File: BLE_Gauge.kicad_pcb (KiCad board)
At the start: 4 copper layers, 53.3 x 50.2 mm, 31 parts, among them J1 TagConnect_TC2030-NL, J2 USB_C_Receptacle_PowerOnly_6P, U1 nRF54L15-QFXX, U2 LSM6DS3, X1 32MHz, X2 32.768kHz

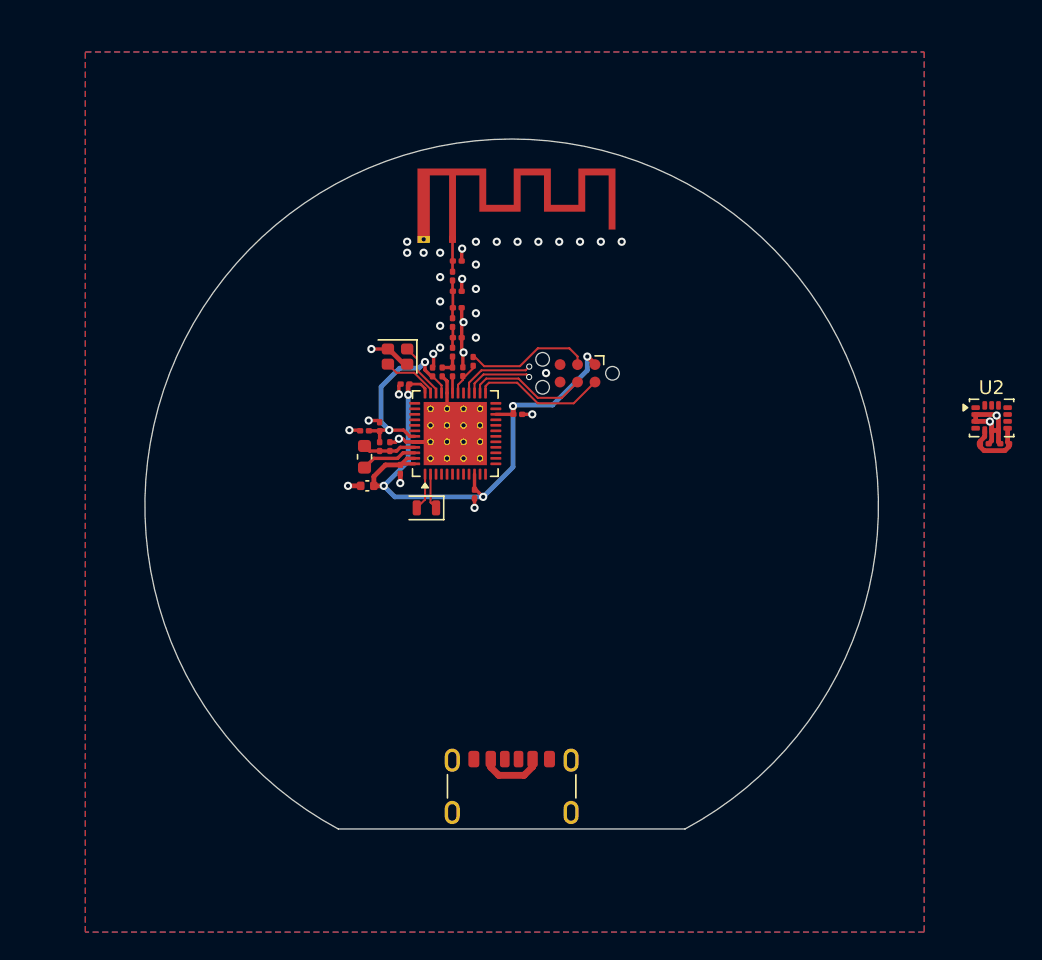
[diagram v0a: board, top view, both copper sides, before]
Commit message: Add Display
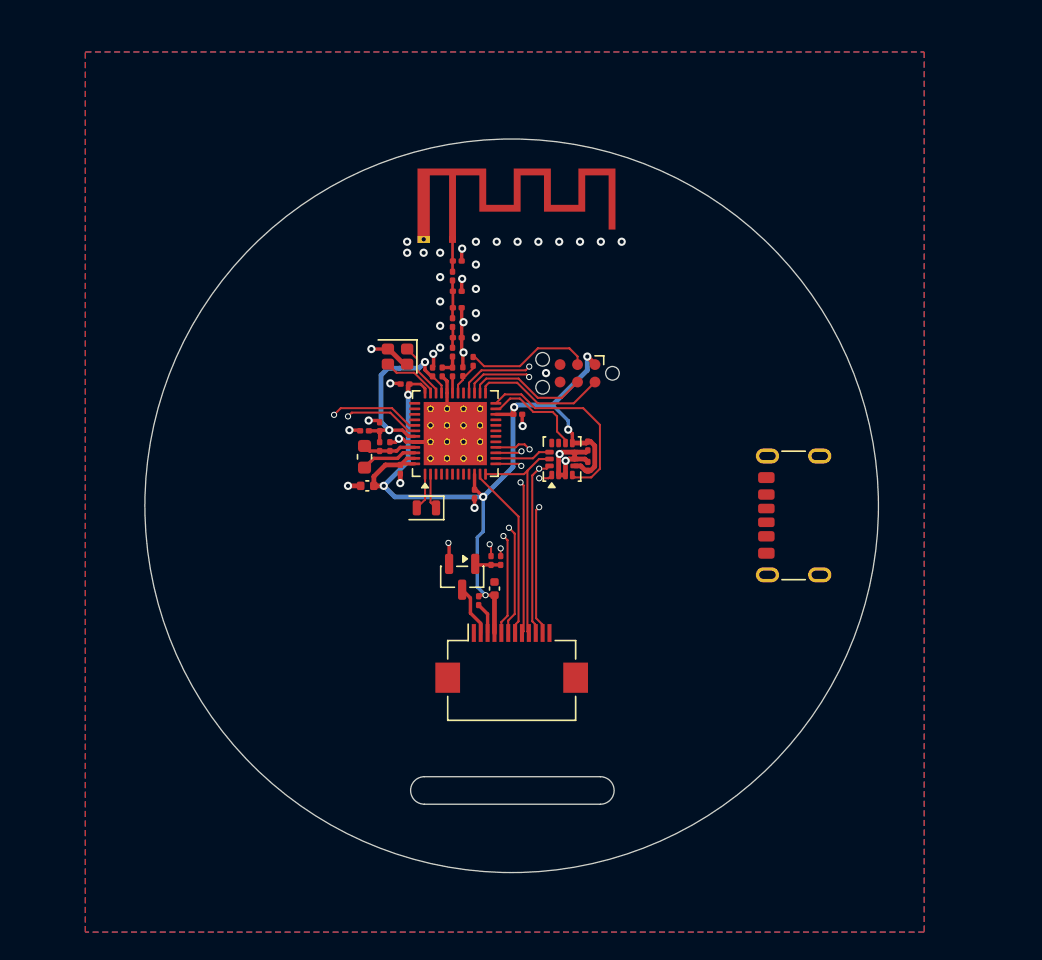
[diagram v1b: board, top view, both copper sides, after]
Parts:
- added C16: 10uF, Capacitor_SMD:C_0402_1005Metric, F.Cu at (147.2, 111.0)
- added J3: Conn_01x12_MountingPin, Connector_FFC-FPC:Hirose_FH12-12S-0.5SH_1x12-1MP_P0.50mm_Horizontal, F.Cu at (148.5, 116.1)
- added Q1: SS8050, Package_TO_SOT_SMD:SOT-23, F.Cu at (144.9, 110.2)
- added R2: 5.1k, Resistor_SMD:R_0201_0603Metric, F.Cu at (146.1, 111.9)
- added R3: 2.2k, Resistor_SMD:R_0201_0603Metric, F.Cu at (147.7, 109.0)
- added R4: 10k, Resistor_SMD:R_0201_0603Metric, F.Cu at (147.0, 109.0)
- moved U2 31.4 mm to (152.2, 101.6), turned to 90 degrees
- moved C15 30.3 mm to (154.0, 100.6), turned to -90 degrees
- moved J2 30.0 mm to (170.1, 105.7), turned to 90 degrees
- moved C14 28.9 mm to (154.0, 102.1), turned to 90 degrees
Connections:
- U1 pad 11: unconnected-(U1-P2.00-Pad11) -> /DC.DISP
- U1 pad 12: unconnected-(U1-P2.01-Pad12) -> /SPI_SCK
- U1 pad 13: unconnected-(U1-P2.02-Pad13) -> /SPI_MISO
- U1 pad 14: unconnected-(U1-P2.03-Pad14) -> /CS.LSM6
- U1 pad 15: unconnected-(U1-P2.04-Pad15) -> /SPI_MOSI
- U1 pad 16: unconnected-(U1-P2.05-Pad16) -> /CS.DISP
- U1 pad 23: unconnected-(U1-P0.00-Pad23) -> /INT2.LSM6
- U1 pad 24: unconnected-(U1-P0.01-Pad24) -> /INT1.LSM6
- U1 pad 28: unconnected-(U1-P0.03-Pad28) -> /BL.DISP
- U1 pad 29: unconnected-(U1-P0.04-Pad29) -> /INT.nPM
- U1 pad 39: unconnected-(U1-P1.11-Pad39) -> /SDA
- U1 pad 40: unconnected-(U1-P1.12-Pad40) -> /SCL
- U1 pad 41: unconnected-(U1-P1.13-Pad41) -> /RST.DISP
- U1 pad 42: unconnected-(U1-P1.14-Pad42) -> /TE.DISP
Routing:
- net /RST.DISP: track 0.00 -> 40.1 mm, vias 0 -> 2
- net /TE.DISP: track 0.00 -> 34.4 mm, vias 0 -> 2
- net /BL.DISP: track 0.00 -> 20.5 mm, vias 0 -> 2
- net /CS.DISP: track 0.00 -> 17.8 mm, vias 0 -> 2
- net /SPI_MISO: track 0.00 -> 17.3 mm, vias 0 -> 3
- net /SPI_SCK: track 0.00 -> 17.0 mm
- net /SPI_MOSI: track 0.00 -> 16.8 mm, vias 0 -> 2
- net VDD: track 47.9 -> 62.6 mm, vias 5 -> 7
- net /INT1.LSM6: track 0.00 -> 14.3 mm
- net /DC.DISP: track 0.00 -> 12.8 mm
- net /INT2.LSM6: track 0.00 -> 7.49 mm
- net unconnected-(U1-P0.03-Pad28): track 5.61 -> 0.00 mm, vias 1 -> 0
- net Net-(J2-VBUS-PadA9): track 4.70 -> 0.00 mm
- net /CS.LSM6: track 0.00 -> 4.09 mm
- net Net-(J3-Pin_2): track 0.00 -> 3.71 mm
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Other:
- board size 53.3 x 50.2 mm -> 53.3 x 53.3 mm

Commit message: Arrumando bagunça
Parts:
- C1: footprint Capacitor_SMD:C_0402_1005Metric -> Nath:C_0402_1005Metric_Nordic
- C10, C11, C12, C13, C2, C3, C6, C7, C8, C9: footprint Capacitor_SMD:C_0201_0603Metric -> Nath:C_0201_0603Metric_Nordic
- C4: value 3.9pF -> 2.2uF; footprint Capacitor_SMD:C_0201_0603Metric -> Nath:C_0201_0603Metric_Nordic
- C5: value 2.2uF -> 3.9pF; footprint Capacitor_SMD:C_0201_0603Metric -> Nath:C_0201_0603Metric_Nordic
- FB1: value 100R@100MHz -> 120R/0.2A; footprint Inductor_SMD:L_0201_0603Metric -> Nath:L_0201_0603Metric_Nordic
- L1: footprint Inductor_SMD:L_0603_1608Metric -> Nath:L_0603_1608Metric_Nordic
- L2, L3, L4: footprint Inductor_SMD:L_0201_0603Metric -> Nath:L_0201_0603Metric_Nordic
- R1: footprint Resistor_SMD:R_0201_0603Metric -> Nath:R_0201_0603Metric_Nordic
- moved J2 25.5 mm to (149.7, 121.0), turned to 0 degrees
- moved J3 16.3 mm to (160.5, 105.1), turned to 90 degrees
- moved R2 11.8 mm to (156.6, 106.7)
- moved Q1 10.5 mm to (155.3, 109.4), turned to 90 degrees
- moved C6 10.0 mm to (148.4, 96.3), turned to 90 degrees
- moved C16 8.88 mm to (154.8, 106.3), turned to 180 degrees
- moved C5 8.62 mm to (144.8, 93.8)
- moved C2 8.50 mm to (141.4, 94.4), turned to 180 degrees
- moved C13 6.95 mm to (143.2, 93.8)
- moved R4 6.22 mm to (153.0, 110.6), turned to -90 degrees
- moved C4 5.72 mm to (140.5, 98.8)
- moved R3 5.31 mm to (153.0, 109.1)
- moved C14 4.69 mm to (156.9, 98.4)
- moved C15 4.65 mm to (156.9, 97.0)
- moved U2 4.38 mm to (155.0, 98.3)
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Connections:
- net Net-(C11-Pad1) renamed /RF
- C1 pad 1: VDD -> VDD_NRF
- C2 pad 1: VDD -> VDD_NRF
- C3 pad 1: VDD -> VDD_NRF
- C4 pad 1: Net-(U1-~{RESET}) -> Net-(U1-DECD)
- C5 pad 1: Net-(U1-DECD) -> Net-(U1-~{RESET})
- C6 pad 1: VDD -> VDD_NRF
- C8 pad 1: VDD -> VDD_NRF
- U1 pad 10: VDD -> VDD_NRF
- U1 pad 22: VDD -> VDD_NRF
- U1 pad 36: VDD -> VDD_NRF
- U1 pad 47: VDD -> VDD_NRF
- U1 pad 48: VDD -> VDD_NRF
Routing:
- net VDD_NRF: track 0.00 -> 31.6 mm, vias 0 -> 4
- net VDD: track 62.6 -> 33.4 mm, vias 7 -> 5
- net GND: track 36.4 -> 23.8 mm, vias 39 -> 72
- net /RST.DISP: track 40.1 -> 32.5 mm
- net /INT.nPM: track 0.00 -> 5.41 mm
- net /SCL: track 0.00 -> 4.54 mm
- net /CS.LSM6: track 4.09 -> 8.60 mm, vias 0 -> 2
- net /SDA: track 0.00 -> 4.51 mm
- net unconnected-(U1-P1.10-Pad38): track 0.00 -> 4.48 mm
- net unconnected-(U1-P1.09-Pad37): track 0.00 -> 4.45 mm
- net /BL.DISP: track 20.5 -> 24.6 mm
- net Net-(U1-DECA): track 15.0 -> 11.2 mm
- net unconnected-(U1-P1.07-Pad8): track 0.00 -> 3.45 mm
- net unconnected-(U1-P1.02-Pad3): track 0.00 -> 3.33 mm
- net unconnected-(U1-P1.03-Pad4): track 0.00 -> 3.29 mm
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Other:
- outline, holes or cut-outs redrawn
- rule pad_to_mask_clearance: 0 -> 0.04

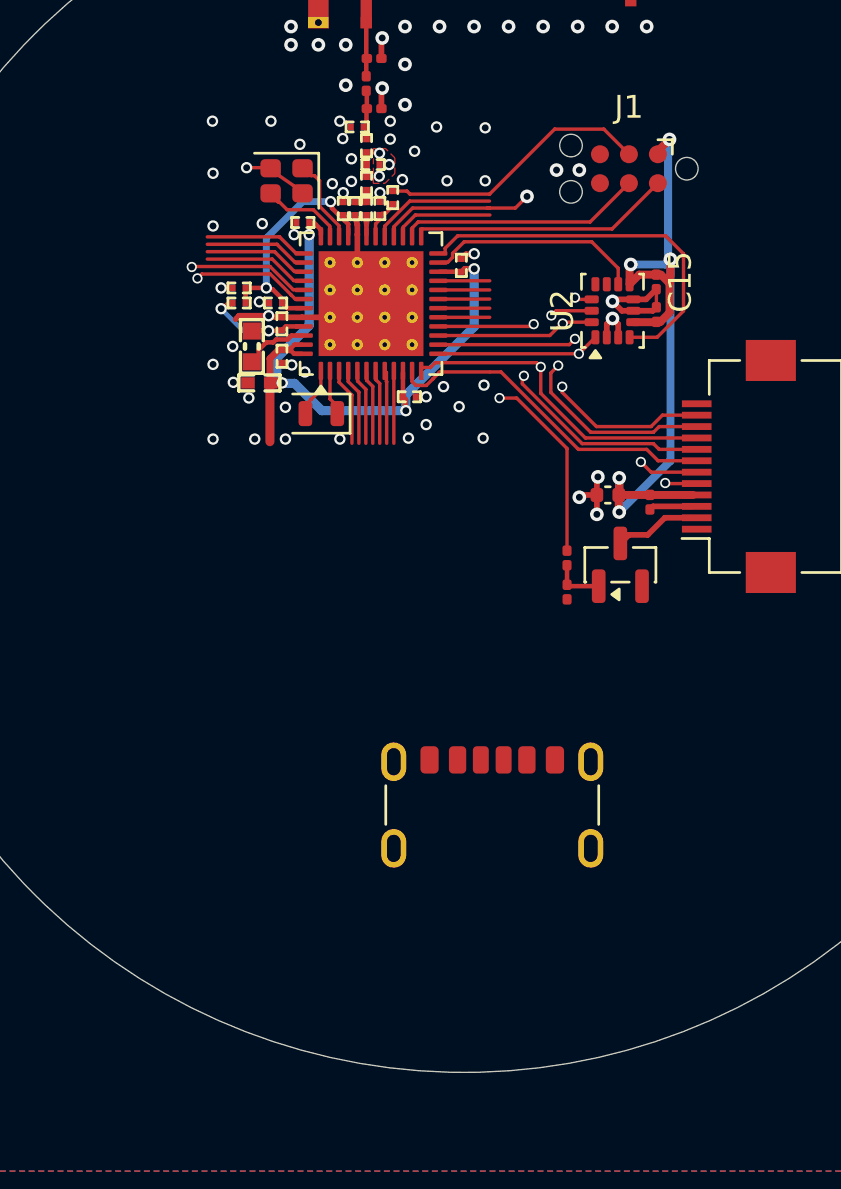
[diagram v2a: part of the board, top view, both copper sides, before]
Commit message: Add PMIC
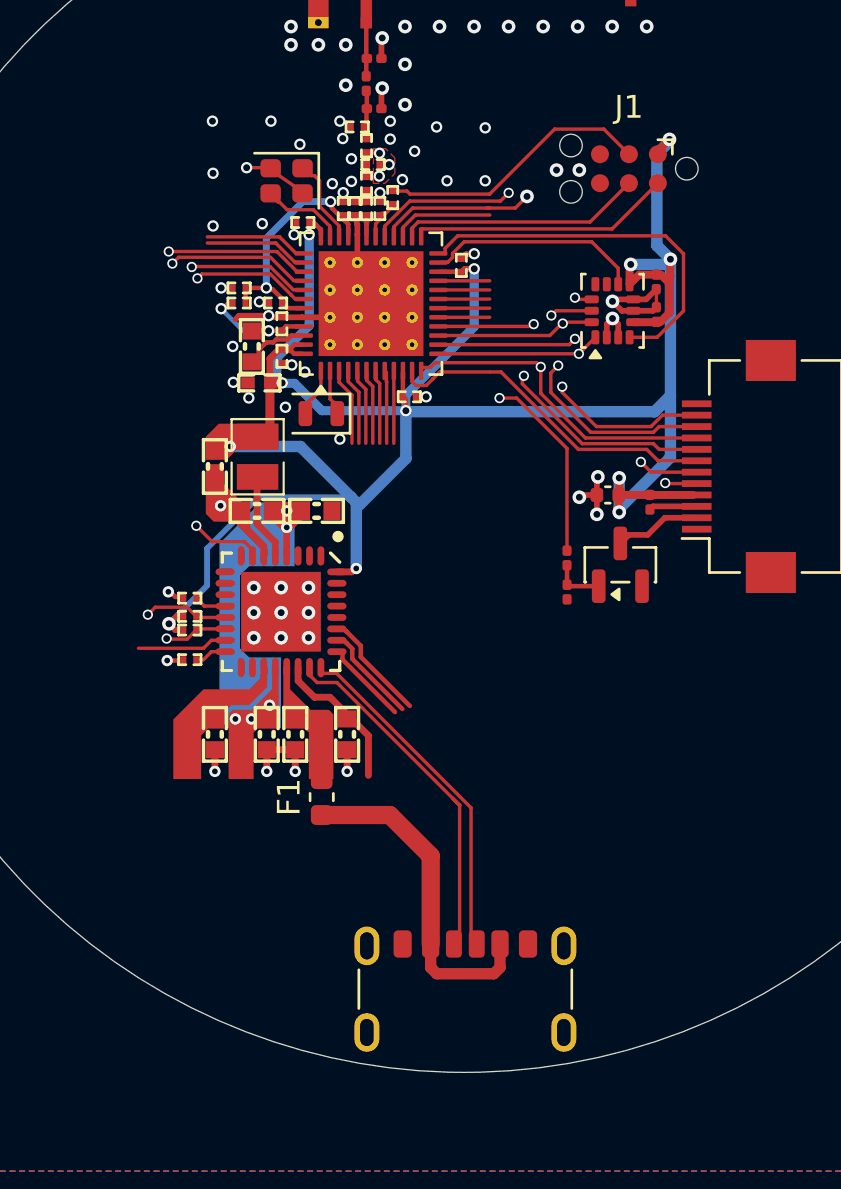
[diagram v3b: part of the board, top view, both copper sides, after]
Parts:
- added C17: 1uF, Nath:C_0603_1608Metric_Nordic, F.Cu at (141.1, 116.8)
- added C18: 100nF, Nath:C_0201_0603Metric_Nordic, F.Cu at (136.5, 110.9)
- added C19: 10uF, Nath:C_0603_1608Metric_Nordic, F.Cu at (142.0, 107.0)
- added C20: 10uF, Nath:C_0603_1608Metric_Nordic, F.Cu at (139.4, 107.0)
- added C21: 10uF, Nath:C_0603_1608Metric_Nordic, F.Cu at (139.8, 116.8)
- added C22: 1uF, Nath:C_0603_1608Metric_Nordic, F.Cu at (143.4, 116.8)
- added C24: 2.2uF, Nath:C_0603_1608Metric_Nordic, F.Cu at (137.6, 116.8)
- added C28: 10uF, Nath:C_0603_1608Metric_Nordic, F.Cu at (137.6, 105.1)
- added F1: 0.5A, Fuse:Fuse_0603_1608Metric, F.Cu at (142.2, 119.6)
- added L6: 2.2uH, Nath:L_0806_2016Metric_Nordic, F.Cu at (139.4, 104.7)
- added R6: 4.7kR, Nath:R_0201_0603Metric_Nordic, F.Cu at (136.5, 112.3)
- added R7: 250kR, Nath:R_0201_0603Metric_Nordic, F.Cu at (136.5, 113.6)
- added R8: 4.7kR, Nath:R_0201_0603Metric_Nordic, F.Cu at (136.5, 111.7)
- added U3: nPM1300-QEAA, Nath:Nordic_QFN50P500X500X90-33N, F.Cu at (140.5, 111.5)
- moved J2 8.16 mm to (148.5, 129.1)
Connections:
- C1 pad 1: VDD_NRF -> +3V3
- C14 pad 1: VDD -> +3V3
- C15 pad 1: VDD -> +3V3
- C16 pad 1: VDD -> +3V3
- C2 pad 1: VDD_NRF -> +3V3
- C3 pad 1: VDD_NRF -> +3V3
- C6 pad 1: VDD_NRF -> +3V3
- C8 pad 1: VDD_NRF -> +3V3
- J1 pad 1: VDD -> +3V3
- J2 pad A5: unconnected-(J2-CC1-PadA5) -> /CC1
- J2 pad B5: unconnected-(J2-CC2-PadB5) -> /CC2
- J3 pad 4: VDD -> +3V3
- R2 pad 2: VDD -> +3V3
- U1 pad 10: VDD_NRF -> +3V3
- U1 pad 22: VDD_NRF -> +3V3
- U1 pad 36: VDD_NRF -> +3V3
- U1 pad 47: VDD_NRF -> +3V3
- U1 pad 48: VDD_NRF -> +3V3
- U2 pad 5: VDD -> +3V3
- U2 pad 8: VDD -> +3V3
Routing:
- net +3V3: track 0.00 -> 108.4 mm, vias 0 -> 12
- net VDD: track 33.4 -> 0.00 mm, vias 5 -> 0
- net VDD_NRF: track 31.6 -> 0.00 mm, vias 4 -> 0
- net /INT.nPM: track 5.41 -> 37.0 mm, vias 0 -> 2
- net /SDA: track 4.51 -> 26.3 mm, vias 0 -> 2
- net /SCL: track 4.54 -> 25.9 mm, vias 0 -> 2
- net /CC1: track 0.00 -> 15.9 mm
- net /CC2: track 0.00 -> 15.3 mm
- net Net-(F1-Pad1): track 0.00 -> 14.7 mm
- net Net-(U3-VBUSOUT): track 0.00 -> 6.40 mm
- net GND: track 23.8 -> 29.9 mm, vias 72 -> 78
- net Net-(D1-BK): track 0.00 -> 4.89 mm
- net Net-(D1-GK): track 0.00 -> 4.39 mm
- net /SHPHLD: track 0.00 -> 3.94 mm
- net Net-(D1-RK): track 0.00 -> 3.82 mm
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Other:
- rule pad_to_mask_clearance: 0.04 -> 0.0762

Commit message: Arrumando Bagunça 2
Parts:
- U3: footprint Nath:Nordic_QFN50P500X500X90-33N -> Package_DFN_QFN:QFN-32-1EP_5x5mm_P0.5mm_EP3.6x3.6mm_ThermalVias
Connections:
- net /VBUS renamed VBUS
- net Net-(D1-BK) renamed /LED2
- net Net-(D1-GK) renamed /LED1
- net Net-(D1-RK) renamed /LED0
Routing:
- net GND: track 29.9 -> 36.2 mm, vias 78 -> 75
- net Net-(U3-VBUSOUT): track 6.40 -> 3.54 mm
- net +3V3: track 108.4 -> 109.1 mm, vias 12 -> 14
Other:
- rule pad_to_mask_clearance: 0.0762 -> 0.05
